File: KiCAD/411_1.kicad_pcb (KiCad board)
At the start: 2 copper layers, 70 x 70 mm, 28 parts, among them U1 MCP6L04-xST, U2 LA72914V-TLM-H, U3 LM78L05_SO8, U5 ATtiny85V-10S

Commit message: Rev 1.0 shipped to oshpark
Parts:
- added C16: 100n, Capacitor_SMD:C_0603_1608Metric_Pad1.08x0.95mm_HandSolder, F.Cu at (200.2, 75.7)
- added C17: 470n, Capacitor_THT:C_Radial_D5.0mm_H5.0mm_P2.00mm, F.Cu at (196.4, 75.6)
- added C18: 1u, Capacitor_THT:C_Radial_D5.0mm_H5.0mm_P2.00mm, F.Cu at (197.5, 68.8)
- added C19: 1u, Capacitor_SMD:C_0603_1608Metric_Pad1.08x0.95mm_HandSolder, F.Cu at (187.7, 71.3)
- added C20: 22u, Capacitor_SMD:C_0805_2012Metric_Pad1.18x1.45mm_HandSolder, F.Cu at (158.4, 96.2)
- added C21: 470p, Capacitor_SMD:C_0603_1608Metric_Pad1.08x0.95mm_HandSolder, F.Cu at (196.7, 93.8)
- added C22: 22u, Capacitor_SMD:C_0805_2012Metric_Pad1.18x1.45mm_HandSolder, F.Cu at (158.4, 100.3)
- added C23: 22u, Capacitor_SMD:C_0805_2012Metric_Pad1.18x1.45mm_HandSolder, F.Cu at (158.4, 98.3)
- added C24: 470p, Capacitor_SMD:C_0603_1608Metric_Pad1.08x0.95mm_HandSolder, F.Cu at (196.7, 99.0)
- added C25: 470p, Capacitor_SMD:C_0603_1608Metric_Pad1.08x0.95mm_HandSolder, F.Cu at (190.9, 101.3)
- added C26: 470p, Capacitor_SMD:C_0603_1608Metric_Pad1.08x0.95mm_HandSolder, F.Cu at (186.1, 101.3)
- added C27: 100n, Capacitor_SMD:C_0603_1608Metric_Pad1.08x0.95mm_HandSolder, F.Cu at (167.2, 104.2)
- added J1: Conn_Coaxial, Connector_Coaxial:U.FL_Molex_MCRF_73412-0110_Vertical, F.Cu at (187.7, 84.1)
- added J2: Conn_Coaxial, Connector_Coaxial:SMA_Amphenol_132134_Vertical, B.Cu at (179.2, 90.8)
- added J3: Conn_Coaxial, Connector_Coaxial:U.FL_Molex_MCRF_73412-0110_Vertical, F.Cu at (191.7, 96.3)
- added J4: Conn_01x05, Connector_PinSocket_2.54mm:PinSocket_1x05_P2.54mm_Vertical, F.Cu at (173.2, 105.4)
- added JP1: Jumper_3_Open, Jumper:SolderJumper-3_P1.3mm_Open_Pad1.0x1.5mm, F.Cu at (171.7, 86.8)
- added JP2: Jumper, Jumper:SolderJumper-2_P1.3mm_Open_RoundedPad1.0x1.5mm, F.Cu at (192.9, 78.2)
- added JP3: Jumper, Jumper:SolderJumper-2_P1.3mm_Open_RoundedPad1.0x1.5mm, F.Cu at (185.0, 90.8)
- added JP4: Jumper, Jumper:SolderJumper-2_P1.3mm_Open_RoundedPad1.0x1.5mm, F.Cu at (191.2, 71.3)
- added JP5: Jumper, Jumper:SolderJumper-2_P1.3mm_Open_RoundedPad1.0x1.5mm, F.Cu at (191.2, 68.8)
- added JP6: Jumper, Jumper:SolderJumper-2_P1.3mm_Open_RoundedPad1.0x1.5mm, F.Cu at (186.1, 97.5)
- added JP7: Connector_PinHeader_1.00mm:PinHeader_1x02_P1.00mm_Vertical, Connector_PinSocket_2.54mm:PinSocket_1x02_P2.54mm_Vertical, F.Cu at (159.4, 103.7)
- added JP8: Jumper_2_Bridged, Connector_PinSocket_2.54mm:PinSocket_1x02_P2.54mm_Vertical, F.Cu at (159.4, 107.2)
- added L1: 220n, Capacitor_SMD:C_0603_1608Metric_Pad1.08x0.95mm_HandSolder, F.Cu at (187.7, 91.6)
- added L2: 220n, Capacitor_SMD:C_0603_1608Metric_Pad1.08x0.95mm_HandSolder, F.Cu at (190.9, 88.3)
- added L3: 220n, Capacitor_SMD:C_0603_1608Metric_Pad1.08x0.95mm_HandSolder, F.Cu at (192.4, 82.9)
- added L4: 3.3u, Capacitor_SMD:C_0603_1608Metric_Pad1.08x0.95mm_HandSolder, F.Cu at (195.8, 96.5)
- added L5: 3.3u, Capacitor_SMD:C_0603_1608Metric_Pad1.08x0.95mm_HandSolder, F.Cu at (193.4, 100.5)
- added L6: 3.3u, Capacitor_SMD:C_0603_1608Metric_Pad1.08x0.95mm_HandSolder, F.Cu at (188.5, 100.5)
- added R10: 10k, Resistor_SMD:R_0603_1608Metric_Pad0.98x0.95mm_HandSolder, F.Cu at (195.1, 64.0)
- added R11: 10k, Resistor_SMD:R_0603_1608Metric_Pad0.98x0.95mm_HandSolder, F.Cu at (192.9, 64.0)
- added R12: 10k, Resistor_SMD:R_0603_1608Metric_Pad0.98x0.95mm_HandSolder, F.Cu at (178.1, 102.9)
- added R13: 10k, Resistor_SMD:R_0603_1608Metric_Pad0.98x0.95mm_HandSolder, F.Cu at (162.8, 97.4)
- added R4: 10k, Resistor_SMD:R_0603_1608Metric_Pad0.98x0.95mm_HandSolder, F.Cu at (169.8, 60.0)
- added R7: 10k, Resistor_SMD:R_0603_1608Metric_Pad0.98x0.95mm_HandSolder, F.Cu at (173.5, 81.8)
- added R8: 10k, Resistor_SMD:R_0603_1608Metric_Pad0.98x0.95mm_HandSolder, F.Cu at (177.2, 81.8)
- added R9: 1k, Resistor_SMD:R_0603_1608Metric_Pad0.98x0.95mm_HandSolder, F.Cu at (200.2, 95.7)
- added RV1: 0-100k, Potentiometer_SMD:Potentiometer_Bourns_3314R-1_Vertical_Hole, F.Cu at (179.6, 62.0)
- added RV2: 0-100k, Potentiometer_SMD:Potentiometer_Bourns_3314R-1_Vertical_Hole, F.Cu at (187.5, 63.5)
- added RV3: 0-100k, Potentiometer_SMD:Potentiometer_Bourns_3314R-1_Vertical_Hole, F.Cu at (166.1, 112.8)
- added RV4: 0-100k, Potentiometer_SMD:Potentiometer_Bourns_3314R-1_Vertical_Hole, F.Cu at (163.8, 66.4)
- added SW1: SW_Push, Connector_PinSocket_2.54mm:PinSocket_1x02_P2.54mm_Vertical, F.Cu at (180.8, 104.5)
- added TP1: Testpoint, Connector_PinHeader_1.00mm:PinHeader_1x01_P1.00mm_Vertical, F.Cu at (168.0, 76.2)
- added TP10: Testpoint, Connector_PinHeader_1.00mm:PinHeader_1x01_P1.00mm_Vertical, F.Cu at (174.1, 80.0)
- added TP11: Testpoint, Connector_PinHeader_1.00mm:PinHeader_1x01_P1.00mm_Vertical, F.Cu at (184.3, 76.7)
- added TP12: Testpoint, Connector_PinHeader_1.00mm:PinHeader_1x01_P1.00mm_Vertical, F.Cu at (162.2, 90.6)
- added TP13: Testpoint, Connector_PinHeader_1.00mm:PinHeader_1x01_P1.00mm_Vertical, F.Cu at (170.1, 110.1)
- added TP14: Testpoint, Connector_PinHeader_1.00mm:PinHeader_1x01_P1.00mm_Vertical, F.Cu at (154.9, 103.7)
- added TP15: Testpoint, Connector_PinHeader_1.00mm:PinHeader_1x01_P1.00mm_Vertical, F.Cu at (167.3, 70.9)
- added TP16: Testpoint, Connector_PinHeader_1.00mm:PinHeader_1x01_P1.00mm_Vertical, F.Cu at (199.8, 71.7)
- added TP17: Testpoint, Connector_PinHeader_1.00mm:PinHeader_1x01_P1.00mm_Vertical, F.Cu at (210.2, 83.5)
- added TP2: Testpoint, Connector_PinHeader_1.00mm:PinHeader_1x01_P1.00mm_Vertical, F.Cu at (189.8, 116.0)
- added TP3: Testpoint, Connector_PinHeader_1.00mm:PinHeader_1x01_P1.00mm_Vertical, F.Cu at (180.8, 69.0)
- added TP4: Testpoint, Connector_PinHeader_1.00mm:PinHeader_1x01_P1.00mm_Vertical, F.Cu at (172.0, 60.9)
- added TP5: Testpoint, Connector_PinHeader_1.00mm:PinHeader_1x01_P1.00mm_Vertical, F.Cu at (196.3, 78.0)
- added TP6: Testpoint, Connector_PinHeader_1.00mm:PinHeader_1x01_P1.00mm_Vertical, F.Cu at (170.7, 90.2)
- added TP7: Testpoint, Connector_PinHeader_1.00mm:PinHeader_1x01_P1.00mm_Vertical, F.Cu at (187.2, 87.9)
- added TP8: Testpoint, Connector_PinHeader_1.00mm:PinHeader_1x01_P1.00mm_Vertical, F.Cu at (186.1, 94.8)
- added TP9: Testpoint, Connector_PinHeader_1.00mm:PinHeader_1x01_P1.00mm_Vertical, F.Cu at (203.2, 77.2)
- added U4: LA72914V-TLM-H, Package_SO:TSSOP-16_4.4x5mm_P0.65mm, F.Cu at (199.2, 82.9)
- BT1: footprint Connector_JST:JST_ACH_BM01B-ACHSS-A-GAN-ETF_1x01-1MP_P1.20mm_Vertical -> Connector_JST:JST_SH_BM02B-SRSS-TB_1x02-1MP_P1.00mm_Vertical
- C1: value TBD -> 1u; footprint Capacitor_SMD:C_0805_2012Metric -> Capacitor_SMD:C_0603_1608Metric_Pad1.08x0.95mm_HandSolder
- C10: value 100n -> 1u; footprint Capacitor_SMD:C_0805_2012Metric -> Capacitor_THT:C_Radial_D5.0mm_H5.0mm_P2.00mm
- C11, C15, C7: footprint Capacitor_SMD:C_0805_2012Metric -> Capacitor_SMD:C_0603_1608Metric_Pad1.08x0.95mm_HandSolder
- C12: value 470n -> 100n; footprint Capacitor_SMD:C_0805_2012Metric -> Capacitor_SMD:C_0603_1608Metric_Pad1.08x0.95mm_HandSolder
- C13: value 470n -> 10n; footprint Capacitor_SMD:C_0805_2012Metric -> Capacitor_SMD:C_0603_1608Metric_Pad1.08x0.95mm_HandSolder
- C14: value TBD -> 6.8n; footprint Capacitor_SMD:C_0805_2012Metric -> Capacitor_SMD:C_0603_1608Metric_Pad1.08x0.95mm_HandSolder
- C2: value 1u -> 100n; footprint Capacitor_SMD:C_0805_2012Metric -> Capacitor_SMD:C_0805_2012Metric_Pad1.18x1.45mm_HandSolder
- C3: value TBD -> 100n; footprint Capacitor_SMD:C_0805_2012Metric -> Capacitor_SMD:C_0603_1608Metric_Pad1.08x0.95mm_HandSolder
- C4: value 100n -> 22u; footprint Capacitor_SMD:C_0805_2012Metric -> Capacitor_SMD:C_0805_2012Metric_Pad1.18x1.45mm_HandSolder
- C5: value 1u -> 5.6n; footprint Capacitor_SMD:C_0805_2012Metric -> Capacitor_SMD:C_0603_1608Metric_Pad1.08x0.95mm_HandSolder
- C6: value 100n -> 5.6n; footprint Capacitor_SMD:C_0805_2012Metric -> Capacitor_SMD:C_0603_1608Metric_Pad1.08x0.95mm_HandSolder
- C8: value 10n -> 5.6n; footprint Capacitor_SMD:C_0805_2012Metric -> Capacitor_SMD:C_0603_1608Metric_Pad1.08x0.95mm_HandSolder
- C9: value 6.8n -> 100n; footprint Capacitor_SMD:C_0805_2012Metric -> Capacitor_SMD:C_0603_1608Metric_Pad1.08x0.95mm_HandSolder
- LS1, MK1: footprint Connector_PinHeader_1.00mm:PinHeader_1x02_P1.00mm_Vertical -> Connector_PinSocket_2.54mm:PinSocket_1x02_P2.54mm_Vertical
- R1: footprint Resistor_SMD:R_0805_2012Metric -> Resistor_SMD:R_0603_1608Metric_Pad0.98x0.95mm_HandSolder
- R2, R3, R5, R6: value TBD -> 10k; footprint Resistor_SMD:R_0805_2012Metric -> Resistor_SMD:R_0603_1608Metric_Pad0.98x0.95mm_HandSolder
- U1: value MCP6L04-xST -> LM2937IMP; footprint Package_SO:TSSOP-14_4.4x5mm_P0.65mm -> Package_TO_SOT_SMD:SOT-223-3_TabPin2
- U2: value LA72914V-TLM-H -> MCP6L04x-xSL; footprint Package_SO:TSSOP-16-1EP_4.4x5mm_P0.65mm -> Package_SO:SOIC-14_3.9x8.7mm_P1.27mm
- U3: value LM78L05_SO8 -> TMUX1101; footprint Package_SO:SOIC-8_3.9x4.9mm_P1.27mm -> Package_TO_SOT_SMD:SOT-23-5_HandSoldering
- moved C14 241.2 mm to (199.3, 90.2)
- moved C15 235.7 mm to (197.8, 90.2), turned to 90 degrees
- moved C11 225.8 mm to (203.8, 88.5), turned to 90 degrees
- moved C12 225.8 mm to (200.8, 90.2), turned to 90 degrees
- moved BT1 225.7 mm to (175.5, 120.0)
- moved U5 221.5 mm to (170.8, 99.3), turned to 180 degrees
- moved C10 221.3 mm to (204.7, 82.2), turned to 0 degrees
- moved C13 219.4 mm to (202.3, 90.2), turned to 90 degrees
- moved C4 213.3 mm to (190.5, 118.4), turned to 180 degrees
- moved C5 213.0 mm to (189.4, 91.6)
- moved U1 210.2 mm to (184.8, 115.2)
- moved C8 206.1 mm to (193.9, 82.9), turned to -90 degrees
- moved C2 203.4 mm to (180.2, 119.5), turned to 90 degrees
- moved C6 202.4 mm to (190.9, 84.9)
- moved D1 201.3 mm to (159.4, 92.3), turned to 90 degrees
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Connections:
- C1 pad 2: FM IN -> Net-(C1-Pad2)
- C10 pad 1: GND -> Net-(C10-Pad1)
- C10 pad 2: Net-(C10-Pad2) -> GND
- C11 pad 1: GND -> Net-(C11-Pad1)
- C12 pad 2: Net-(C12-Pad2) -> VCC
- C13 pad 1: Net-(C13-Pad1) -> GND
- C13 pad 2: Net-(C13-Pad2) -> Net-(C11-Pad1)
- C15 pad 2: VCC -> Net-(C15-Pad2)
- C2 pad 1: Net-(C2-Pad1) -> GND
- C2 pad 2: Net-(C2-Pad2) -> Net-(BT1-Pad1)
- C3 pad 1: Net-(C3-Pad1) -> VCC
- C4 pad 1: unconnected-(C4-Pad1) -> GND
- C5 pad 1: GND -> Net-(C5-Pad1)
- C5 pad 2: Net-(C5-Pad2) -> GND
- C7 pad 1: GND -> VCC
- C7 pad 2: VCC -> GND
- C8 pad 1: GND -> Net-(C6-Pad2)
- C8 pad 2: Net-(C6-Pad1) -> GND
- C9 pad 1: GND -> Net-(C9-Pad1)
- D1 pad 1: Net-(C14-Pad2) -> Net-(R13-Pad1)
- MK1 pad 2: Net-(C2-Pad2) -> Net-(C1-Pad2)
- R1 pad 1: Net-(C2-Pad2) -> Net-(C1-Pad2)
- R2 pad 1: GND -> Net-(C1-Pad1)
- R2 pad 2: Net-(R2-Pad2) -> VCC
- R3 pad 1: Net-(R3-Pad1) -> GND
- R3 pad 2: Net-(R2-Pad2) -> Net-(C1-Pad1)
- R5 pad 1: Net-(R5-Pad1) -> VCC
- R5 pad 2: GND -> Net-(JP1-Pad1)
- R6 pad 1: Net-(LS1-Pad1) -> Net-(JP1-Pad3)
- R6 pad 2: Net-(R5-Pad1) -> GND
- U1 pad 1: Net-(R3-Pad1) -> Net-(BT1-Pad1)
- U1 pad 2: Net-(R2-Pad2) -> GND
- U1 pad 3: Net-(C2-Pad1) -> VCC
- U2 pad 1: unconnected-(U2-Pad1) -> Net-(RV1-Pad3)
- U2 pad 10: Net-(C5-Pad2) -> Net-(C19-Pad2)
- U2 pad 11: Net-(C11-Pad2) -> GND
- U2 pad 12: unconnected-(U2-Pad12) -> VCC
- U2 pad 2: Net-(C10-Pad2) -> Net-(RV1-Pad2)
- U2 pad 3: Net-(C9-Pad2) -> Net-(C1-Pad1)
- U2 pad 5: Net-(C3-Pad1) -> Net-(JP5-Pad2)
- U2 pad 6: unconnected-(U2-Pad6) -> Net-(RV4-Pad2)
- U2 pad 7: Net-(C6-Pad1) -> Net-(LS1-Pad1)
- U2 pad 8: Net-(C6-Pad2) -> Net-(D1-Pad2)
- U2 pad 9: Net-(C13-Pad1) -> Net-(RV2-Pad2)
- U3 pad 1: VCC -> Net-(C9-Pad2)
- U3 pad 2: GND -> Net-(RV1-Pad3)
- U3 pad 4: unconnected-(U3-Pad4) -> MIC_EN
- U3 pad 5: unconnected-(U3-Pad5) -> VCC
- U5 pad 1: unconnected-(U5-Pad1) -> /~{RST}
- U5 pad 2: unconnected-(U5-Pad2) -> Net-(R12-Pad2)
- U5 pad 3: unconnected-(U5-Pad3) -> MIC_EN
- U5 pad 5: Net-(C14-Pad2) -> /MOSI
- U5 pad 6: Net-(RV1-Pad2) -> /MISO
- U5 pad 7: unconnected-(U5-Pad7) -> /SCK
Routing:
- net VCC: track 4.41 -> 237.2 mm, vias 0 -> 18
- net MIC_EN: track 0.00 -> 73.1 mm
- net Net-(D1-Pad2): track 0.00 -> 43.9 mm
- net Net-(JP1-Pad2): track 0.00 -> 38.4 mm
- net Net-(JP5-Pad2): track 0.00 -> 31.3 mm, vias 0 -> 2
- net Net-(RV1-Pad3): track 0.00 -> 30.1 mm
- net Net-(LS1-Pad1): track 3.52 -> 31.3 mm
- net Net-(C9-Pad1): track 0.00 -> 27.7 mm, vias 0 -> 2
- net Net-(RV2-Pad2): track 0.00 -> 25.5 mm
- net /MISO: track 0.00 -> 25.1 mm
- net /RF_Rx: track 0.00 -> 24.2 mm
- net Net-(C19-Pad2): track 0.00 -> 23.2 mm
- net /MOSI: track 0.00 -> 21.5 mm
- net Net-(C1-Pad1): track 0.00 -> 18.8 mm
- net Net-(RV1-Pad2): track 0.00 -> 18.2 mm
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- added copper zone on B.Cu, net GND
- added copper zone on F.Cu, net GND
- added copper zone on F.Cu, net VCC
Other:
- rule pad_to_mask_clearance: 0 -> 0.0508
- board text added: "Comp"
- board text added: "Detection"
- board text added: "ECE411 Team 4 RF Tin Can Rev 1 11/18/2021 David Lay, Nick Lekas, Sydney McBee, Garrett Smith(~{Josh}), Josh Horejs"
- board text added: "Mic"
- board text added: "Speaker"
- board text added: "U+23DA"

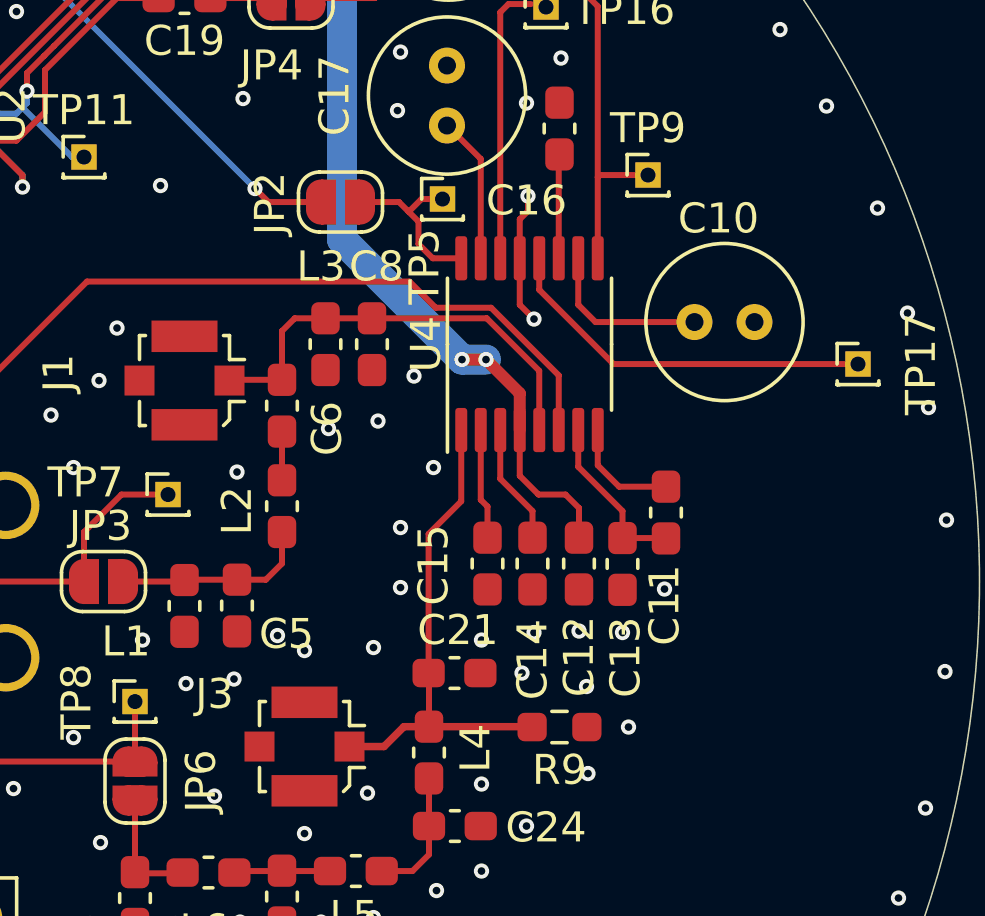
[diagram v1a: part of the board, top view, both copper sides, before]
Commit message: Added info to components for bom generation
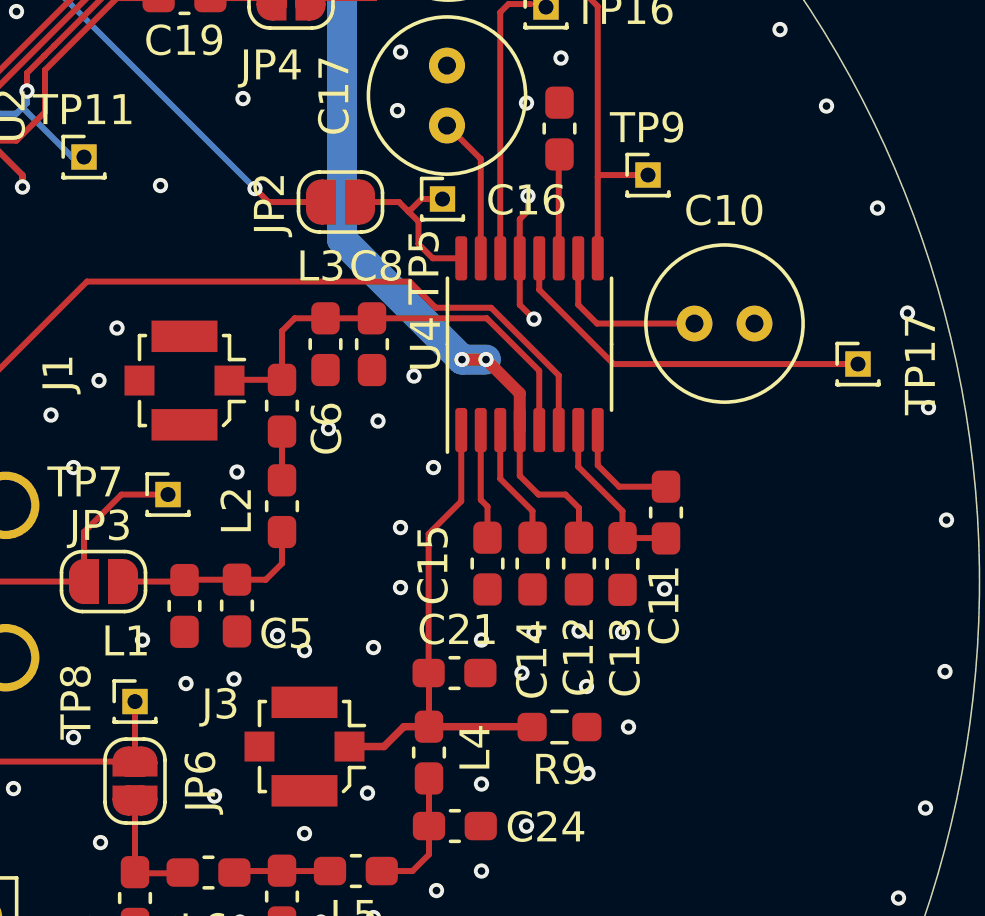
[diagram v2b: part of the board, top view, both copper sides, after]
